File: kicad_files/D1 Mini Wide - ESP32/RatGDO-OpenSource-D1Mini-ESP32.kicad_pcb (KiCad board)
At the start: 2 copper layers, 70 x 55 mm, 13 parts, among them J1 Screw_Terminal_01x03, J2 Screw_Terminal_01x03, J3 Screw_Terminal_01x03, Q1 2N7002, Q2 AO3400A, U1 mini_esp32

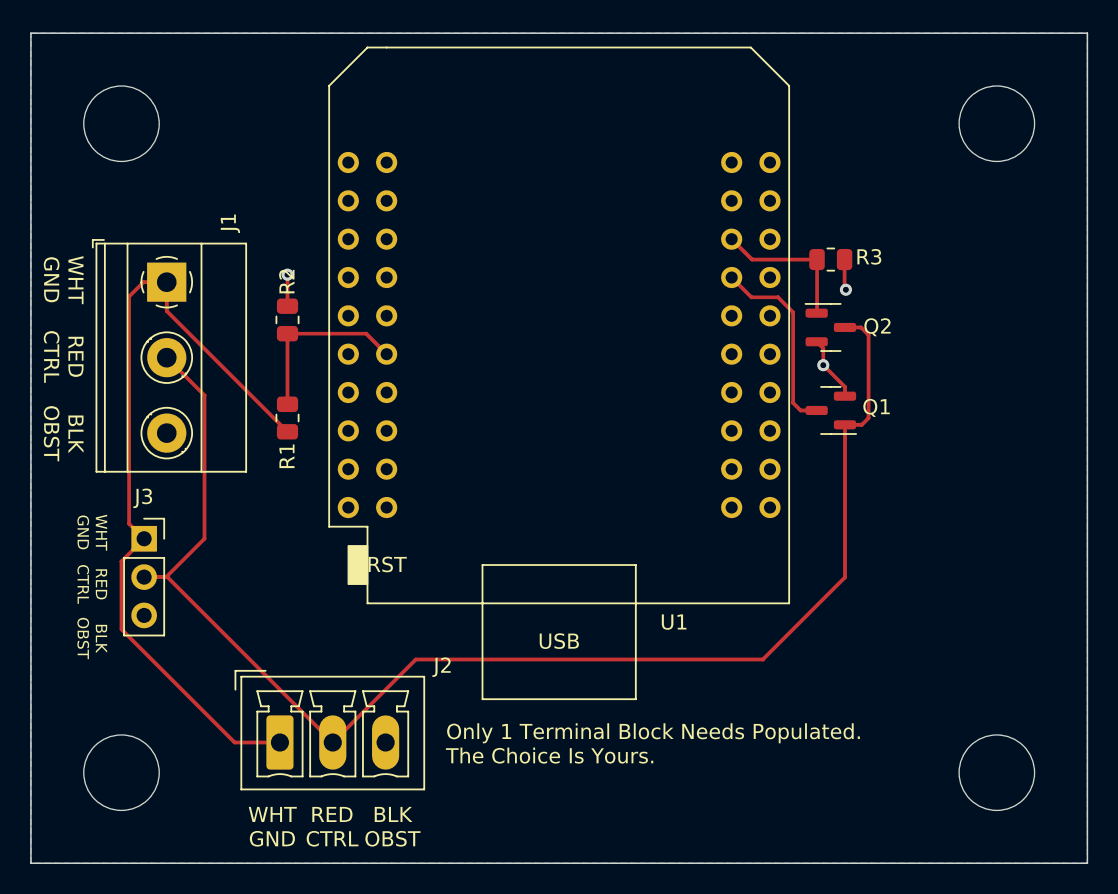
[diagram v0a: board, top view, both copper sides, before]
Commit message: Fixed Silkscreen issue - positive and ground swap
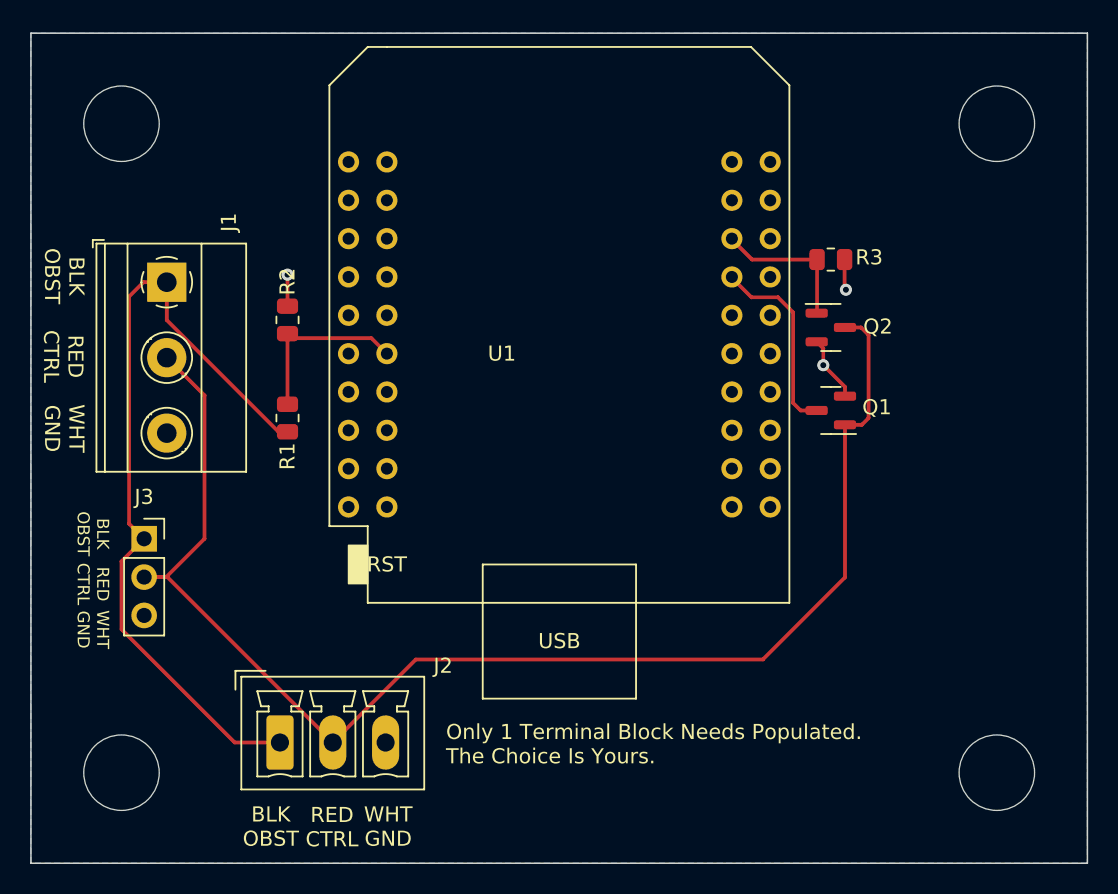
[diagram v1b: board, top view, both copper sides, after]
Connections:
- U1 pad 12: Net-(U2-IO_23/D7) -> Net-(U1-IO_23/D7)
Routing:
- net Net-(U2-IO_23/D7): track 11.8 -> 0.00 mm
- net Net-(U1-IO_23/D7): track 0.00 -> 11.8 mm

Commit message: Update schematics for mini wide board v2.5
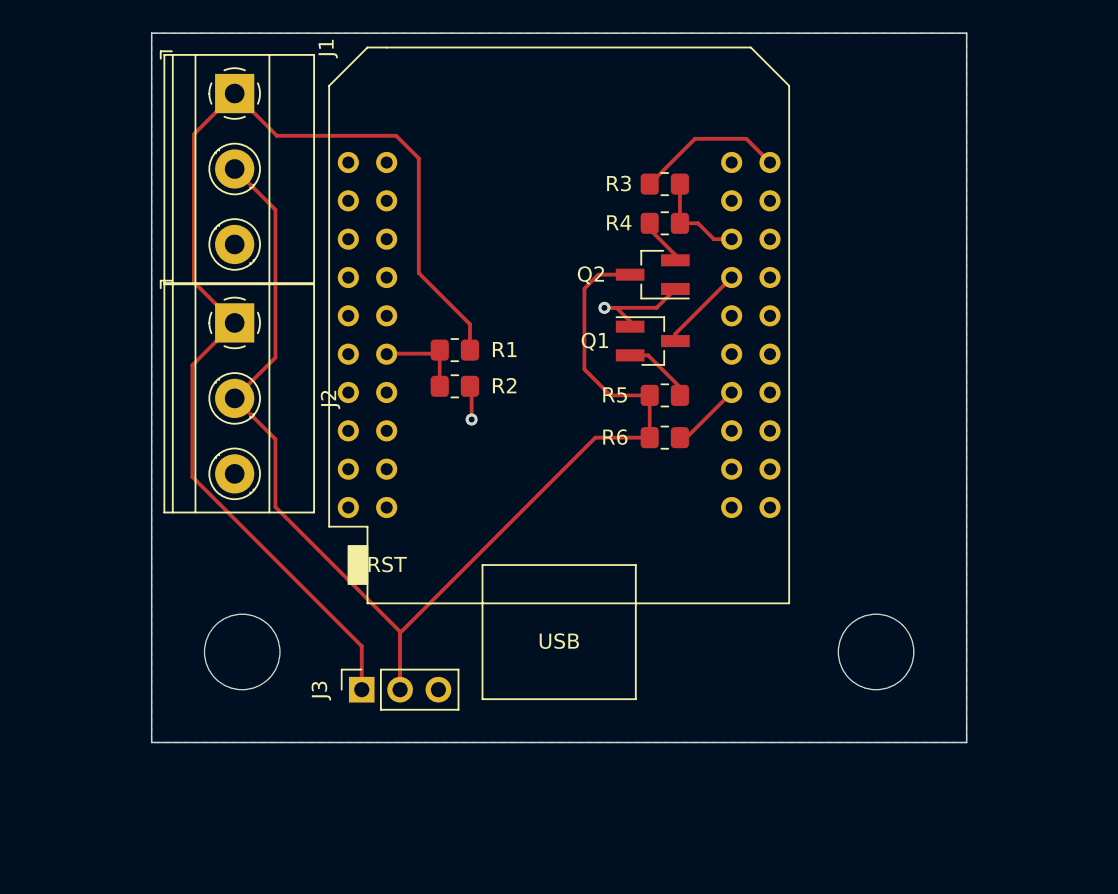
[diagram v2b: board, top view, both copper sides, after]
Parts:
- removed REF** (x2): MountingHole_5mm, MountingHole:MountingHole_5mm
- added R4: 1k, Resistor_SMD:R_0805_2012Metric_Pad1.20x1.40mm_HandSolder, F.Cu at (156.0, 69.6)
- added R5: 10k, Resistor_SMD:R_0805_2012Metric_Pad1.20x1.40mm_HandSolder, F.Cu at (156.0, 81.0)
- added R6: 10k, Resistor_SMD:R_0805_2012Metric_Pad1.20x1.40mm_HandSolder, F.Cu at (156.0, 83.8)
- J2: footprint Connector_Phoenix_MC:PhoenixContact_MCV_1,5_3-G-3.5_1x03_P3.50mm_Vertical -> TerminalBlock_Phoenix:TerminalBlock_Phoenix_MKDS-1,5-3_1x03_P5.00mm_Horizontal
- Q1, Q2: footprint Package_TO_SOT_SMD:SOT-23 -> Package_TO_SOT_SMD:SOT-23_Handsoldering
- R1, R2, R3: footprint Resistor_SMD:R_0805_2012Metric -> Resistor_SMD:R_0805_2012Metric_Pad1.20x1.40mm_HandSolder
- moved J2 23.0 mm to (127.5, 81.2), turned to -90 degrees
- moved J3 19.7 mm to (138.5, 100.5), turned to 90 degrees
- moved Q1 12.7 mm to (155.2, 77.4), turned to 0 degrees
- moved Q2 12.3 mm to (155.2, 73.0), turned to 180 degrees
- moved R3 12.1 mm to (156.0, 67.0)
- moved R1 12.0 mm to (142.1, 78.0), turned to 180 degrees
- moved R2 11.9 mm to (142.1, 80.4), turned to 0 degrees
- moved H1 11.3 mm to (170.0, 98.0)
- moved H1 11.3 mm to (128.0, 98.0)
- moved J1 8.75 mm to (127.5, 66.0)
- renumbered REF** to H1
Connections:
- net Net-(J1-BLK/OBST) renamed BLK/OBST
- net Net-(Q1-D) renamed /ESP_RX
- J1 pad 2: Net-(J1-RED/CTRL) -> RED/CTRL
- J2 pad 2: Net-(J1-RED/CTRL) -> RED/CTRL
- J3 pad 2: Net-(J1-RED/CTRL) -> RED/CTRL
- Q1 pad 1: Net-(J1-RED/CTRL) -> Net-(Q1-G)
- Q2 pad 3: Net-(J1-RED/CTRL) -> RED/CTRL
- R3 pad 1: GND -> /ESP_TX
- R3 pad 2: Net-(Q2-G) -> GND
- U1 pad 1: unconnected-(U1-GND-Pad1) -> GND
- U1 pad 22: unconnected-(U1-GND-Pad22) -> GND
- U1 pad 25: Net-(Q2-G) -> /ESP_TX
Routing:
- net Net-(J1-RED/CTRL): track 92.7 -> 0.00 mm
- net RED/CTRL: track 0.00 -> 83.5 mm
- net BLK/OBST: track 53.2 -> 75.6 mm
- net GND: track 8.50 -> 24.6 mm, vias 3 -> 2
- net /ESP_RX: track 12.8 -> 5.76 mm
- net Net-(Q2-G): track 9.78 -> 3.15 mm
- net /ESP_TX: track 0.00 -> 6.46 mm
- net Net-(U1-IO_23/D7): track 11.8 -> 6.61 mm
- net Net-(Q1-G): track 0.00 -> 4.72 mm
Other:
- board size 70 x 55 mm -> 54 x 47 mm
- board text removed: "Only 1 Terminal Block Needs Populated. The Choice Is Yours."
